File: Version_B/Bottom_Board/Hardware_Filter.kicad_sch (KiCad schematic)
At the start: 38 parts, among them U1 LM324, U2 LM324

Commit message: 1st test for better accuracy
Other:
- title: (none) -> Current Monitoring System
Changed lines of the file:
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@@
 (kicad_sch (version 20230121) (generator eeschema)
   (paper "A4")
+  (title_block
+    (title "Current Monitoring System")
+  )
   (junction (at 88.265 111.125) (diameter 0) (color 0 0 0 0)
   )

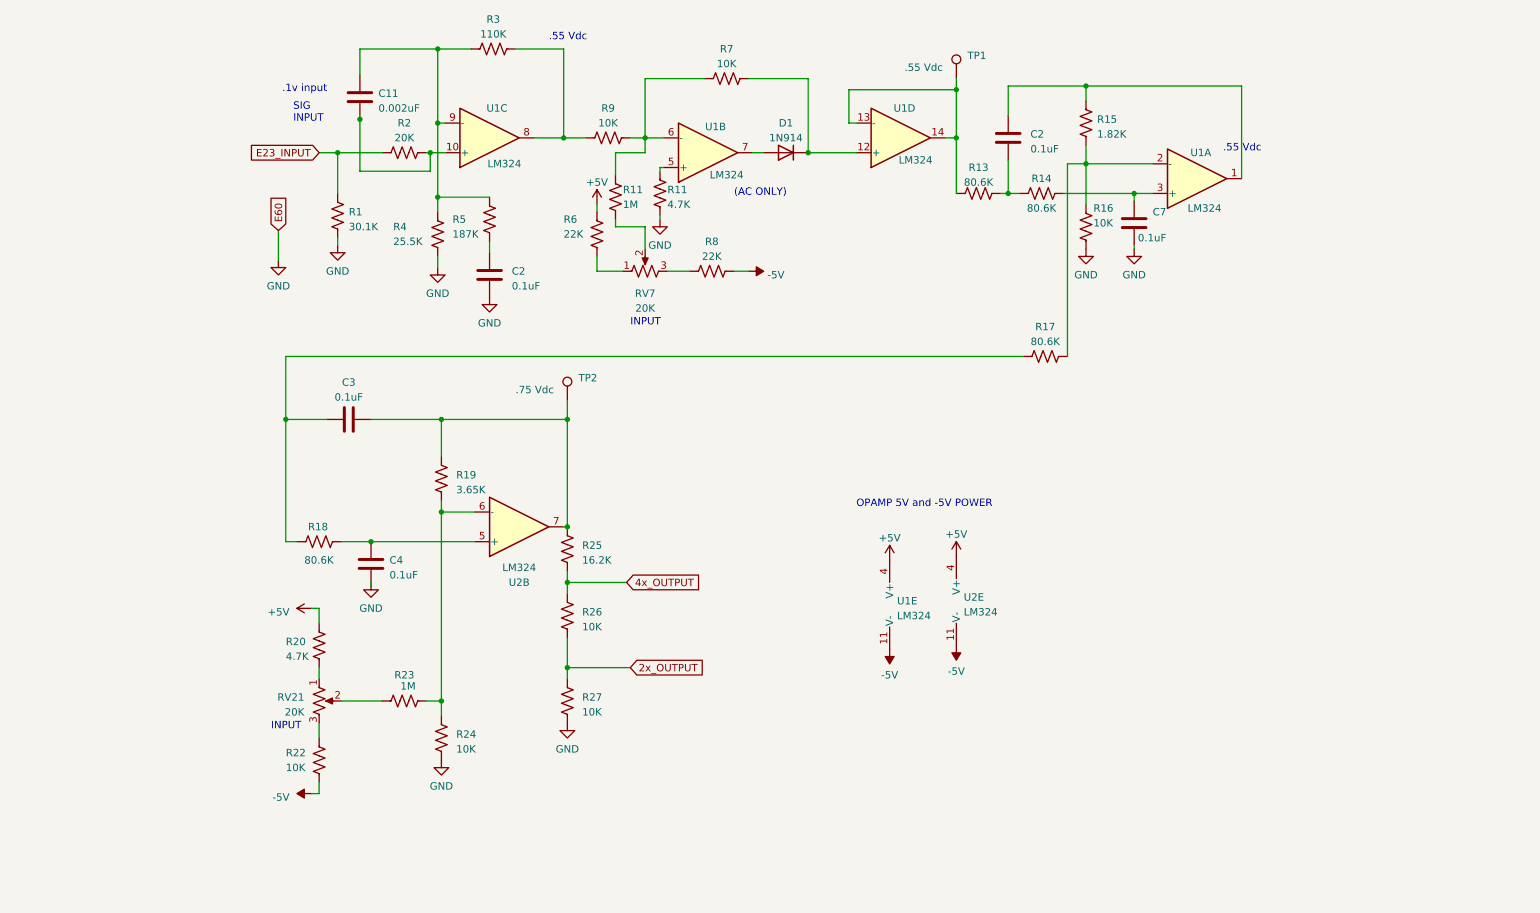
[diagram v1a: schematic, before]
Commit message: ads1015 on bottom board and aesthetic changes
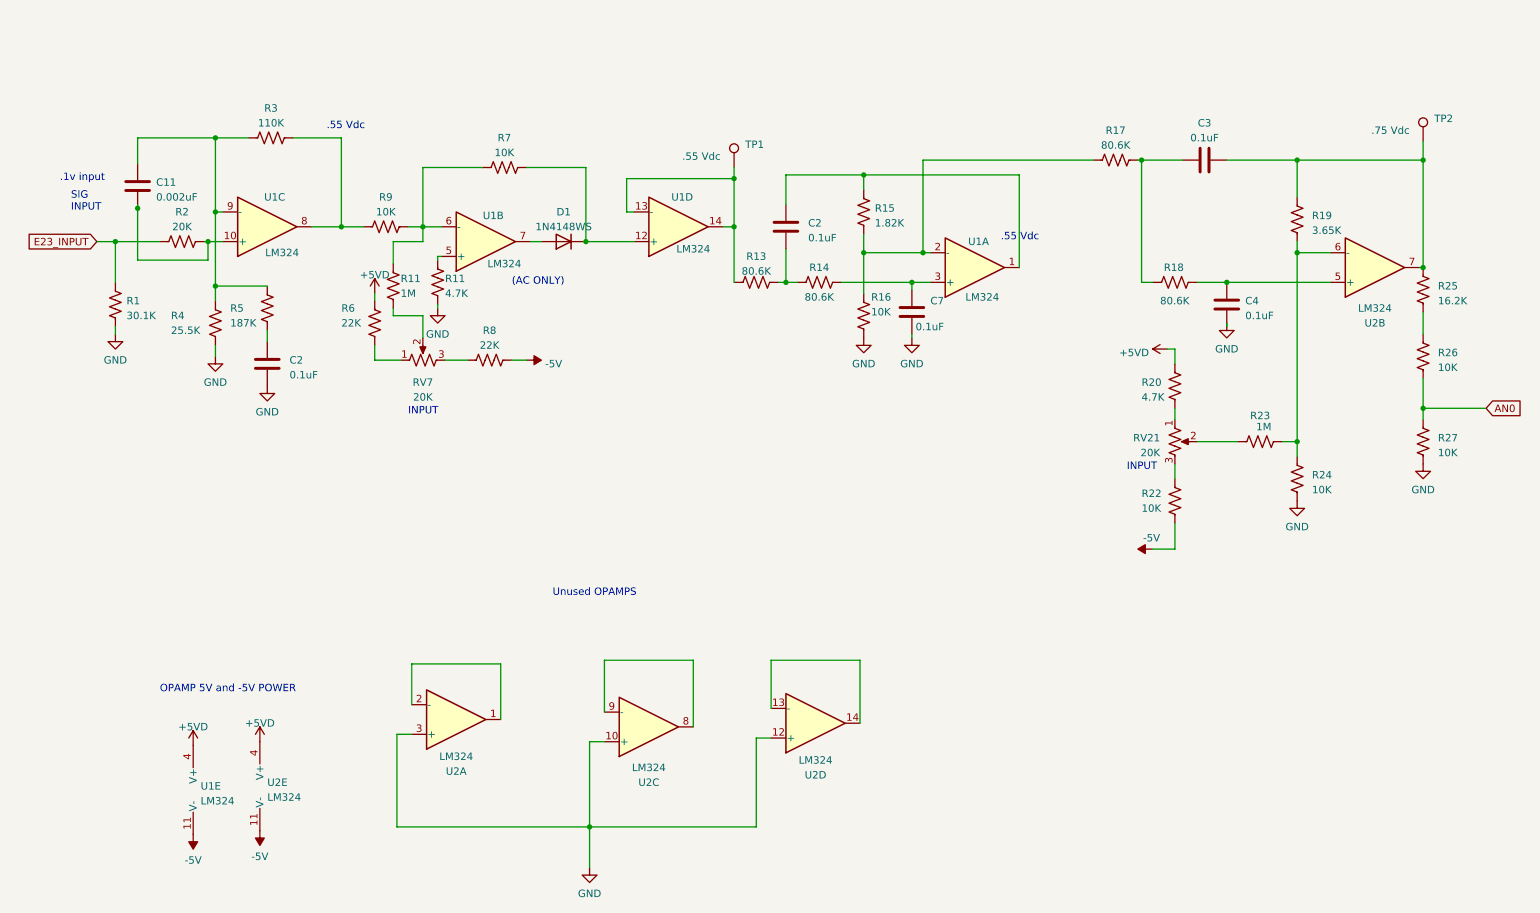
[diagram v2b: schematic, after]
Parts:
- added unit 1 of U2
- added unit 4 of U2
- added unit 3 of U2
- D1: value 1N914 -> 1N4148WS; footprint Diode_SMD:D_0603_1608Metric -> bot_lib:Diode_1N4148WS
- RV21, RV7: footprint Potentiometer_THT:Potentiometer_Bourns_3386P_Vertical -> bot_lib:Potentiometer_Bourns_3386P_Vertical
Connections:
- net GND: now also U2.10 (+), U2.12 (+), U2.3 (+)
- net +5V renamed +5VD
- net 2x_OUTPUT renamed AN0
- net 4x_OUTPUT: no longer names the net of R25.1, R26.2
- new net: U2.1, U2.2 (-)
- new net: U2.13 (-), U2.14
- new net: U2.8, U2.9 (-)
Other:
- note added: "Unused OPAMPS"
- moved on the sheet: C11, C2, C3, C4, C7, D1, R1, R11, R13, R14, R15, R16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
